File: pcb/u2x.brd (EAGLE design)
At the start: 56 x 85 mm, 29 parts, among them IC1 LD117AS33TR, IC2 LD117AS25TR, IC3 LD117AS12TR, SW20 324_SW, U1 USB251XB, U5 CH340C, X1 USB2, X8 USB2

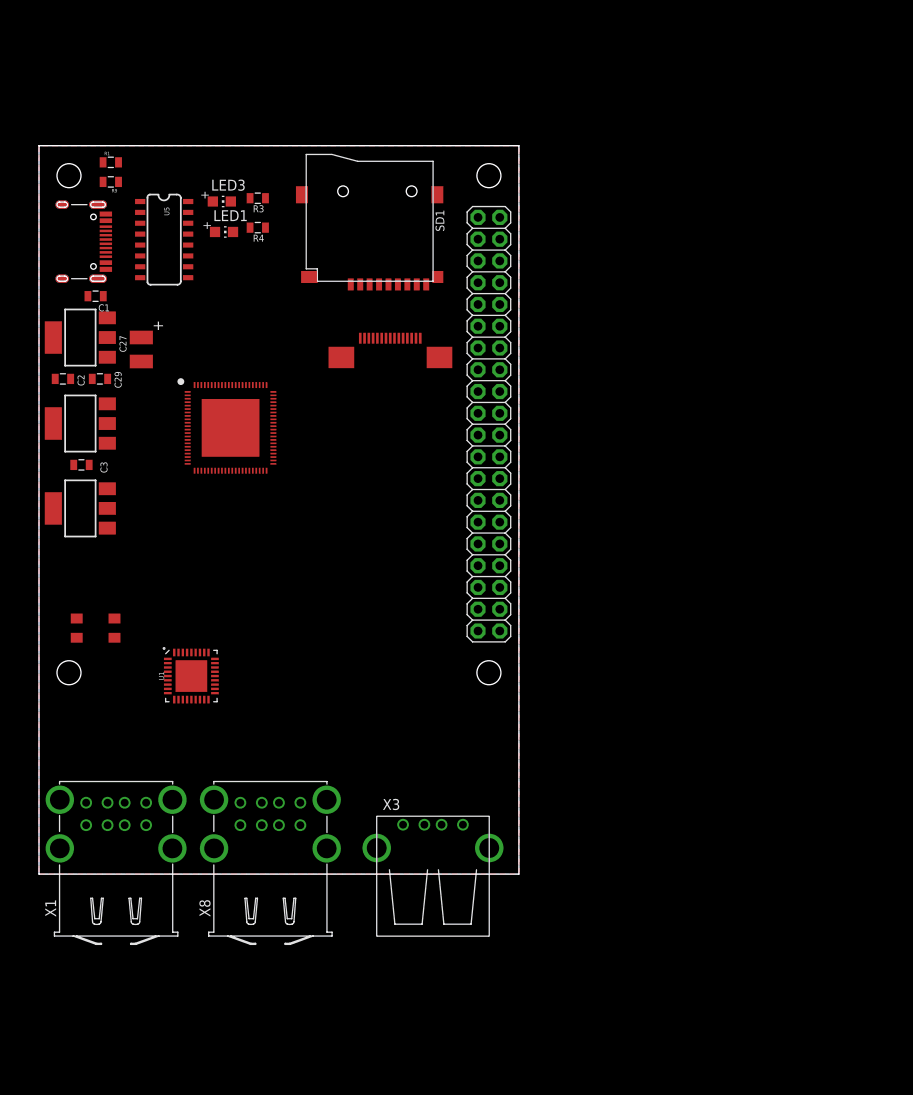
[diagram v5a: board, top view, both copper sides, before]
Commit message: connecting power, sd card, and crystal
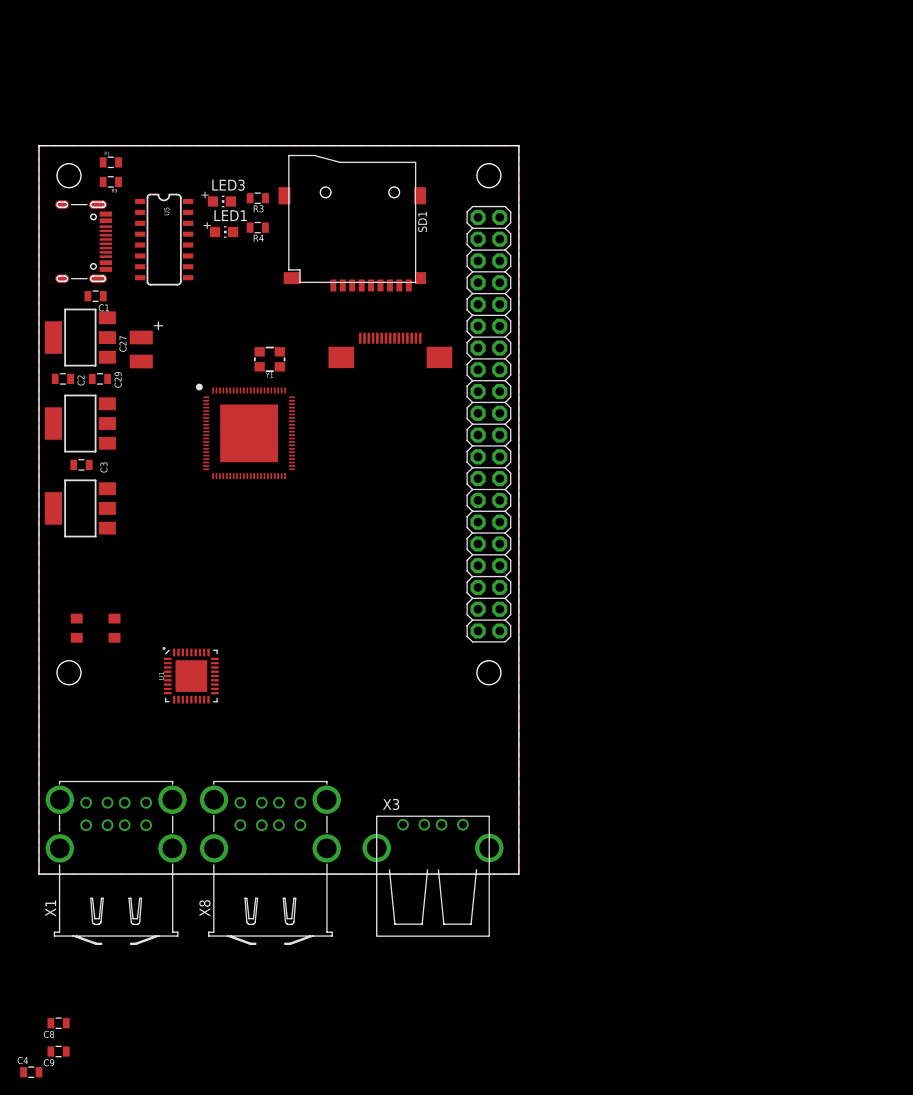
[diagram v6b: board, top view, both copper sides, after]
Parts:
- added C4: 1uF, clock:0805
- added C8, C9: 18pF, clock:0805
- added Y1: 24MHz, SparkFun-Clocks:CRYSTAL-SMD-3.2X2.5MM
- C1, C2, C29, C3: device clock:0805@1 -> clock:0805
- moved U$1 2.25 mm to (24.5, 51.4)
- moved SD1 2.04 mm to (36.6, 76.3)
- turned JP1 to 270 degrees
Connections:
- new net +1V2: C3.2, IC3.4, U$1.P$22, U$1.P$35, U$1.P$71
- new net +2V5: C2.2, IC2.4, U$1.P$30, U$1.P$31, U$1.P$32, U$1.P$34, U$1.P$36, U$1.P$80
- new net N$1: SD1.8, U$1.P$58
- new net N$10: SD1.3, U$1.P$55
- new net N$11: SD1.2, U$1.P$54
- new net N$12: SD1.1, U$1.P$53
- new net N$8: SD1.7, U$1.P$57
- new net N$9: SD1.5, U$1.P$56
- net +3V3: now also C4.2, JP1.1, JP1.17, SD1.4, U$1.P$20, U$1.P$5, U$1.P$50, U$1.P$67, U$1.P$73
- net +5V: now also JP1.2, JP1.4
- net GND: now also C4.1, C8.2, C9.2, JP1.14, JP1.20, JP1.25, JP1.30, JP1.34, JP1.39, JP1.6, JP1.9, SD1.6, SD1.S1, SD1.S2, SD1.S3, SD1.S4, U$1.P$74, U$1.P$82, U$1.P$89, Y1.2, Y1.4
- net N$3: now also C8.1, U$1.P$51, Y1.1; no longer C2.2, IC2.4
- net N$4: now also C9.1, U$1.P$52, Y1.3; no longer C3.2, IC3.4
- net VDD: no longer SD1.4
- net VSS: no longer SD1.6

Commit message: routing traces
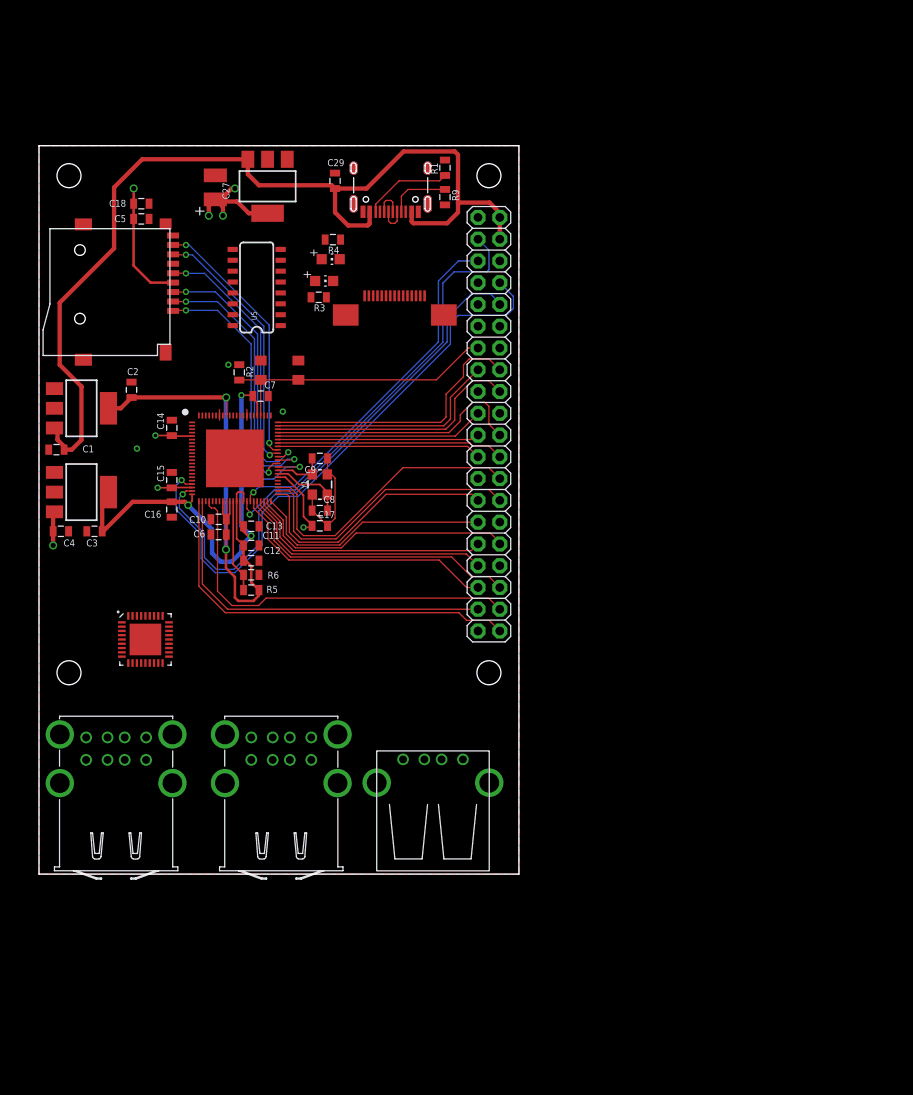
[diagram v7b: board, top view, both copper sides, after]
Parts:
- added C10, C11, C12, C13, C14, C15, C16, C17, C18, C5, C6, C7: 1uF, clock:0805
- added R2, R5, R6: 10K, SparkFun-Passives:0805
- moved C9 75.6 mm to (32.8, 48.5)
- moved C8 67.1 mm to (32.8, 42.4), turned to 180 degrees
- moved C4 63.2 mm to (2.55, 40.0), turned to 180 degrees
- moved R9 39.0 mm to (47.4, 79.0), turned to 270 degrees
- moved R1 39.0 mm to (47.4, 82.4), turned to 90 degrees
- moved SW20 37.0 mm to (28.1, 58.8)
- moved C29 35.9 mm to (34.5, 80.9), turned to 270 degrees
- moved J2 33.4 mm to (41.0, 77.3), turned to 180 degrees
- moved SD1 29.7 mm to (8.03, 67.9), turned to 90 degrees
- moved IC1 28.1 mm to (26.7, 80.3), turned to 180 degrees
- moved C27 20.8 mm to (20.6, 80.1), turned to 90 degrees
- moved C1 18.5 mm to (2.03, 49.5), turned to 0 degrees
- moved Y1 15.7 mm to (32.8, 45.5), turned to 90 degrees
- moved LED3 15.1 mm to (33.3, 69.2)
- moved R3 13.6 mm to (32.6, 67.3)
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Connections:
- new net N$13: U$1.P$68, U1.30
- new net N$14: R5.2, R6.1, U$1.P$33
- new net N$15: U$1.P$69, U1.31
- new net N$16: J2.A6, J2.B6, U5.5
- new net N$17: JP1.13, R2.2, SW20.P$2, SW20.P$3, U$1.P$70
- new net N$18: J2.A7, J2.B7, U5.6
- new net N$19: JP1.26, U$1.P$47
- new net N$20: JP1.28, U$1.P$46
- new net N$21: JP1.27, U$1.P$45
- new net N$22: JP1.18, U$1.P$64
- new net N$23: JP1.22, U$1.P$63
- new net N$24: JP1.15, U$1.P$65
- new net N$25: JP1.16, U$1.P$66
- new net N$26: JP1.29, U$1.P$44
- new net N$27: JP1.32, U$1.P$43
- new net N$28: JP1.31, U$1.P$42
- new net N$29: JP1.33, U$1.P$41
- new net N$30: JP1.36, U$1.P$40
- new net N$31: JP1.35, U$1.P$39
- new net N$32: JP1.38, U$1.P$26
- new net N$33: JP1.40, U$1.P$23
- new net N$34: JP1.37, U$1.P$24
- new net SPI0_CLK: JP1.23, U$1.P$59
- new net SPI0_CS: JP1.24, U$1.P$60
- new net SPI0_MISO: JP1.21, U$1.P$61
- new net SPI0_MOSI: JP1.19, U$1.P$62
- new net TWI0_SCL: JP1.5, U$1.P$38
- new net TWI0_SDA: JP1.3, U$1.P$37
- new net UART0_RX: U$1.P$49, U5.2
- new net UART0_TX: U$1.P$48, U5.3
- new net UART2_RX: JP1.10, U$1.P$21
- new net UART2_TX: JP1.8, U$1.P$19
- net +1V2: now also C13.2, C16.2, C7.2
- net +2V5: now also C10.2, C11.2, C12.2, C6.2, R5.1
- net +3V3: now also C14.2, C15.2, C17.2, C18.2, C5.2, R2.1
- net GND: now also C10.1, C11.1, C12.1, C13.1, C14.1, C15.1, C16.1, C17.1, C18.1, C5.1, C6.1, C7.1, R6.2, SW20.P$1, SW20.P$4
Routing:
- net +5V: track 0.00 -> 115.8 mm
- net UART2_TX: track 0.00 -> 69.2 mm, vias 0 -> 1
- net +2V5: track 0.00 -> 68.3 mm, vias 0 -> 2
- net UART2_RX: track 0.00 -> 62.9 mm, vias 0 -> 1
- net +1V2: track 0.00 -> 56.9 mm, vias 0 -> 3
- net TWI0_SDA: track 0.00 -> 49.6 mm, vias 0 -> 1
- net +3V3: track 0.00 -> 49.1 mm, vias 0 -> 11
- net N$33: track 0.00 -> 47.2 mm
- net N$32: track 0.00 -> 45.6 mm
- net N$34: track 0.00 -> 43.1 mm
- net TWI0_SCL: track 0.00 -> 42.7 mm, vias 0 -> 1
- net N$12: track 0.00 -> 34.5 mm, vias 0 -> 2
- net N$19: track 0.00 -> 34.4 mm
- net N$30: track 0.00 -> 34.0 mm
- net N$20: track 0.00 -> 33.6 mm
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
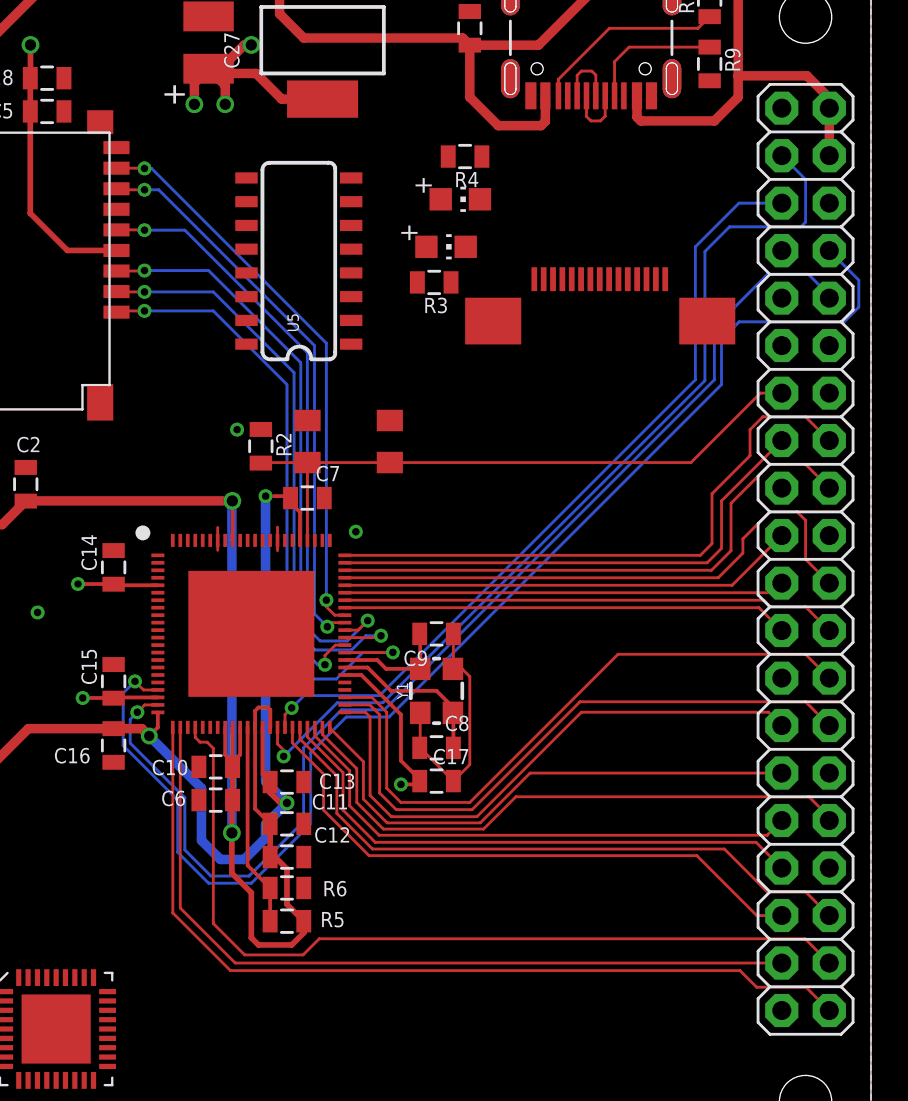
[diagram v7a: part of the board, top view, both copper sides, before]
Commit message: main chip traces done
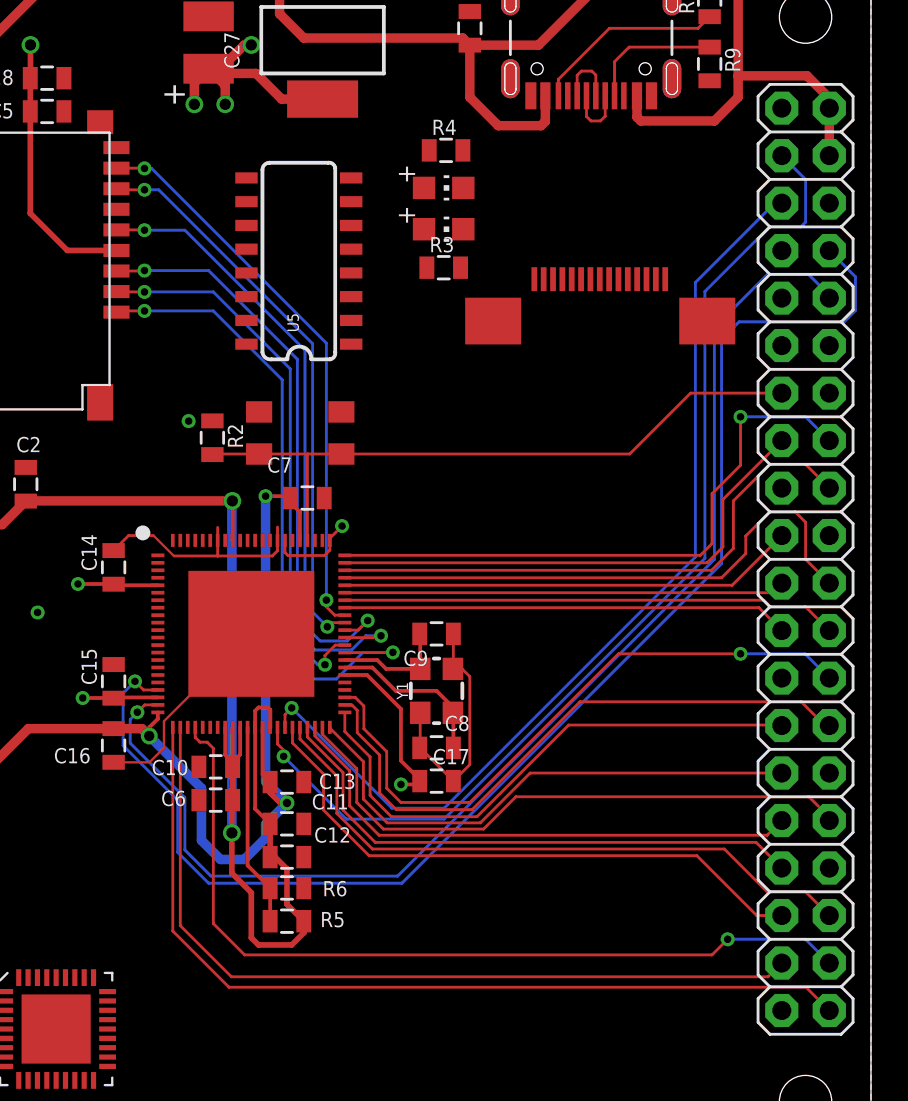
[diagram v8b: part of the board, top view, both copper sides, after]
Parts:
- moved SW20 2.63 mm to (25.5, 59.3)
- moved R2 2.63 mm to (20.8, 59.0)
- moved LED1 1.08 mm to (33.1, 72.4)
- moved R4 1.07 mm to (33.3, 74.4), turned to 0 degrees
- moved LED3 0.95 mm to (33.1, 70.2)
- moved R3 0.94 mm to (33.1, 68.1), turned to 0 degrees
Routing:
- net GND: track 15.8 -> 36.8 mm
- net TWI0_SCL: track 42.7 -> 51.6 mm
- net TWI0_SDA: track 49.6 -> 56.7 mm
- net +3V3: track 49.1 -> 54.0 mm
- net UART2_RX: track 62.9 -> 66.2 mm
- net UART2_TX: track 69.2 -> 72.4 mm
- net N$17: track 33.6 -> 36.5 mm
- net N$21: track 30.7 -> 29.5 mm
- net N$34: track 43.1 -> 44.2 mm
- net N$25: track 31.9 -> 32.6 mm, vias 0 -> 1
- net N$20: track 33.6 -> 33.0 mm
- net N$33: track 47.2 -> 47.8 mm
- net N$19: track 34.4 -> 33.9 mm, vias 0 -> 1
- net N$32: vias 0 -> 1
